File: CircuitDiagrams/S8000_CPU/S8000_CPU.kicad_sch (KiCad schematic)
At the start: 0 parts

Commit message: S8000 CPU schematics Page 3
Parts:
- added U27, U8: 7432, Package_DIP:DIP-14_W7.62mm, symbol 74xx:74LS32
- added U32: 7404, Package_DIP:DIP-14_W7.62mm, symbol 74xx:74LS04
- added U35: 7407, Package_DIP:DIP-14_W7.62mm, symbol 74xx:74LS07
- added U4: 7421, Package_DIP:DIP-14_W7.62mm, symbol 74xx:74LS21
- added U54: 7427, Package_DIP:DIP-14_W7.62mm, symbol 74xx:74LS27
- added U81: 7414, Package_DIP:DIP-14_W7.62mm, symbol 74xx:74LS14
- added U9: 7400, Package_DIP:DIP-14_W7.62mm, symbol 74xx:74LS00
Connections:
- net +5V: now also U27.14 (VCC), U32.14 (VCC), U35.14 (VCC), U4.14 (VCC), U54.14 (VCC), U8.14 (VCC), U81.14 (VCC), U9.14 (VCC)
- net GND: now also U27.7 (GND), U32.7 (GND), U35.7 (GND), U4.7 (GND), U54.7 (GND), U8.7 (GND), U81.7 (GND), U9.7 (GND)
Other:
- added sheet S8000 CPU 03 (S8000_CPU_03.kicad_sch)
- sheet S8000 CPU 02 ports: added none; removed ADIN[0..15], IAD[0..15], IST0, IST1, IST2, IST3, I~{DS}, SEGT

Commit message: Add Page 4
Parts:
- added U14: 74113, Package_DIP:DIP-14_W7.62mm, symbol 74xx:74LS113
- added U33: 7411, Package_DIP:DIP-14_W7.62mm, symbol 74xx:74LS11
- added U41, U42: 7432, Package_DIP:DIP-14_W7.62mm, symbol 74xx:74LS32
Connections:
- net +5V: now also U14.14 (VCC), U33.14 (VCC), U41.14 (VCC), U42.14 (VCC)
- net GND: now also U14.7 (GND), U33.7 (GND), U41.7 (GND), U42.7 (GND)
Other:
- added sheet S8000 CPU 04 (S8000_CPU_04.kicad_sch)
- sheet S8000 CPU 02 ports: added none; removed BUSACKH, BUS_B/~{W}, BUS_N/~{S}, BUS_R/~{W}, BUS_ST0, BUS_ST1, BUS_ST2, BUS_ST3, BUS_ST4, BUS_~{BUSACK}, BUS_~{NMI}, BUS_~{NVI}, BUS_~{REQ}, BUS_~{STOP}, BUS_~{VI}, BUS_~{WAIT}, B/~{W}, CLOCK, IAS, IB/~{W}, IDS, IN/~{S}, IR/~{W}, ISNAD[0..7], IW/~{B}, IW/~{R}, I~{AS}, LAD[0..15], R/~{W}, SN[0..6], ST0, ST1, ST2, ST3, ~{AS}, ~{BD DATAEN}, ~{BUSACK}, ~{DS}, ~{INT}, ~{IST3}, ~{MREQ}, ~{MRESET}, ~{RESET}, ~{SEGT}, ~{SEL_SN_VIOL_REG}, ~{WAIT}
- moved on the sheet: U27E, U32G, U35G

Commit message: Add Page 5 (SIO 0+1)
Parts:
- added U104, U127: 7404, symbol 74xx:74LS04
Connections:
- net +5V: now also U104.14 (VCC), U127.14 (VCC)
- net GND: now also U104.7 (GND), U127.7 (GND)
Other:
- added sheet S8000 CPU 05 (S8000_CPU_05.kicad_sch)
- moved on the sheet: U41E, U42E, U54D, U81G

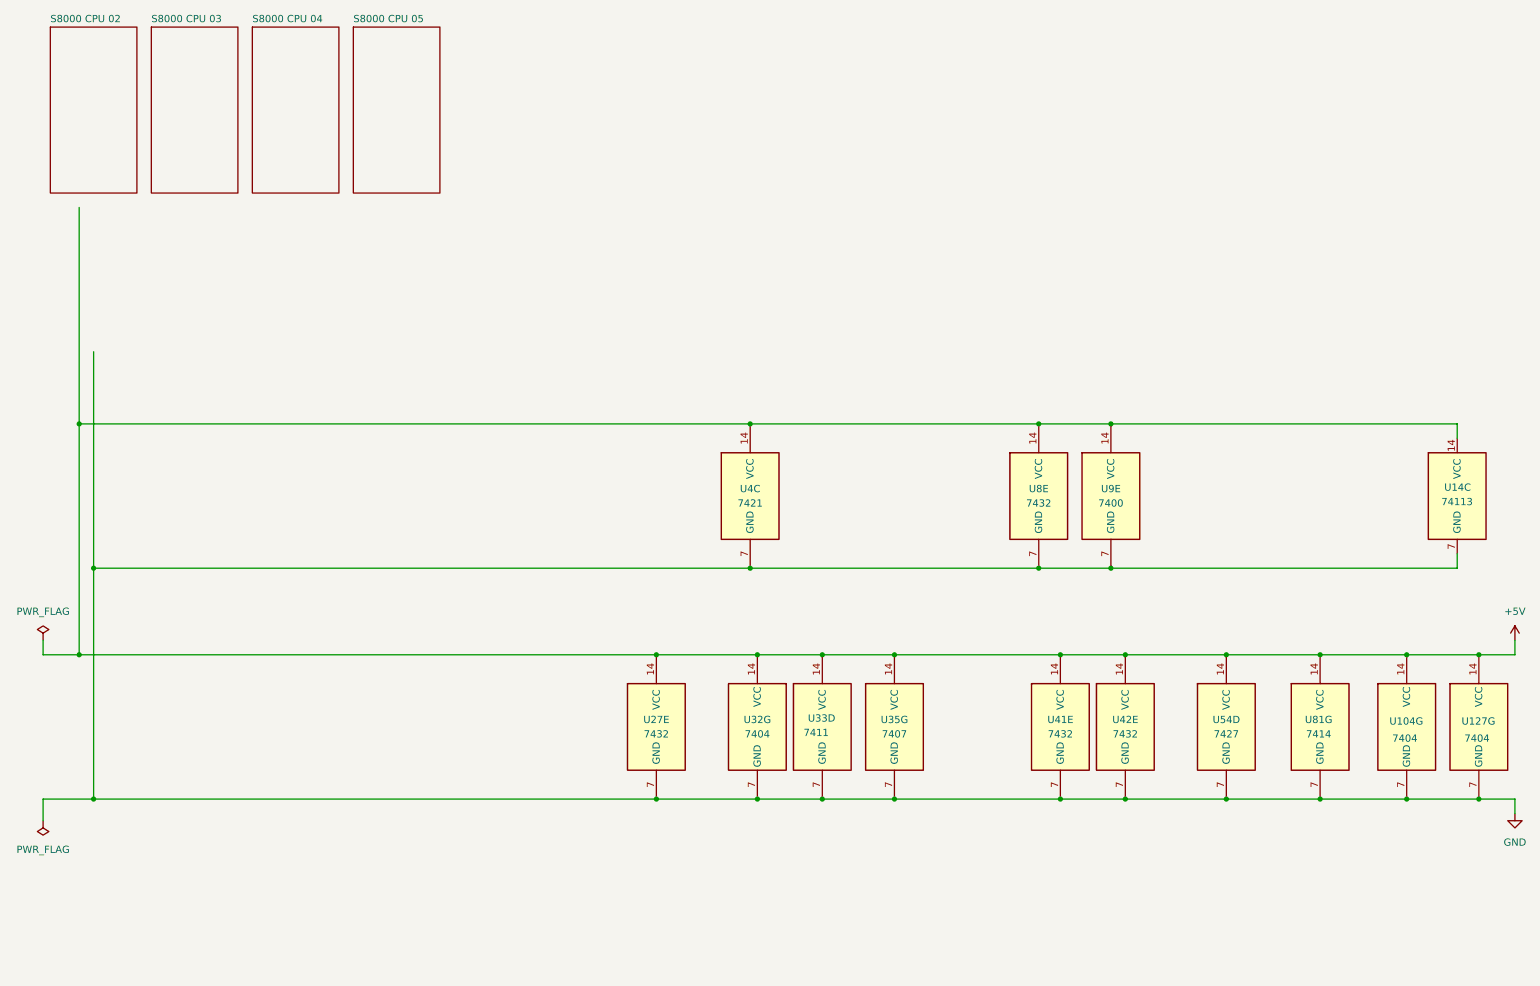
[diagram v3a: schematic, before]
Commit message: Add Page 6 (SIO 2+3)
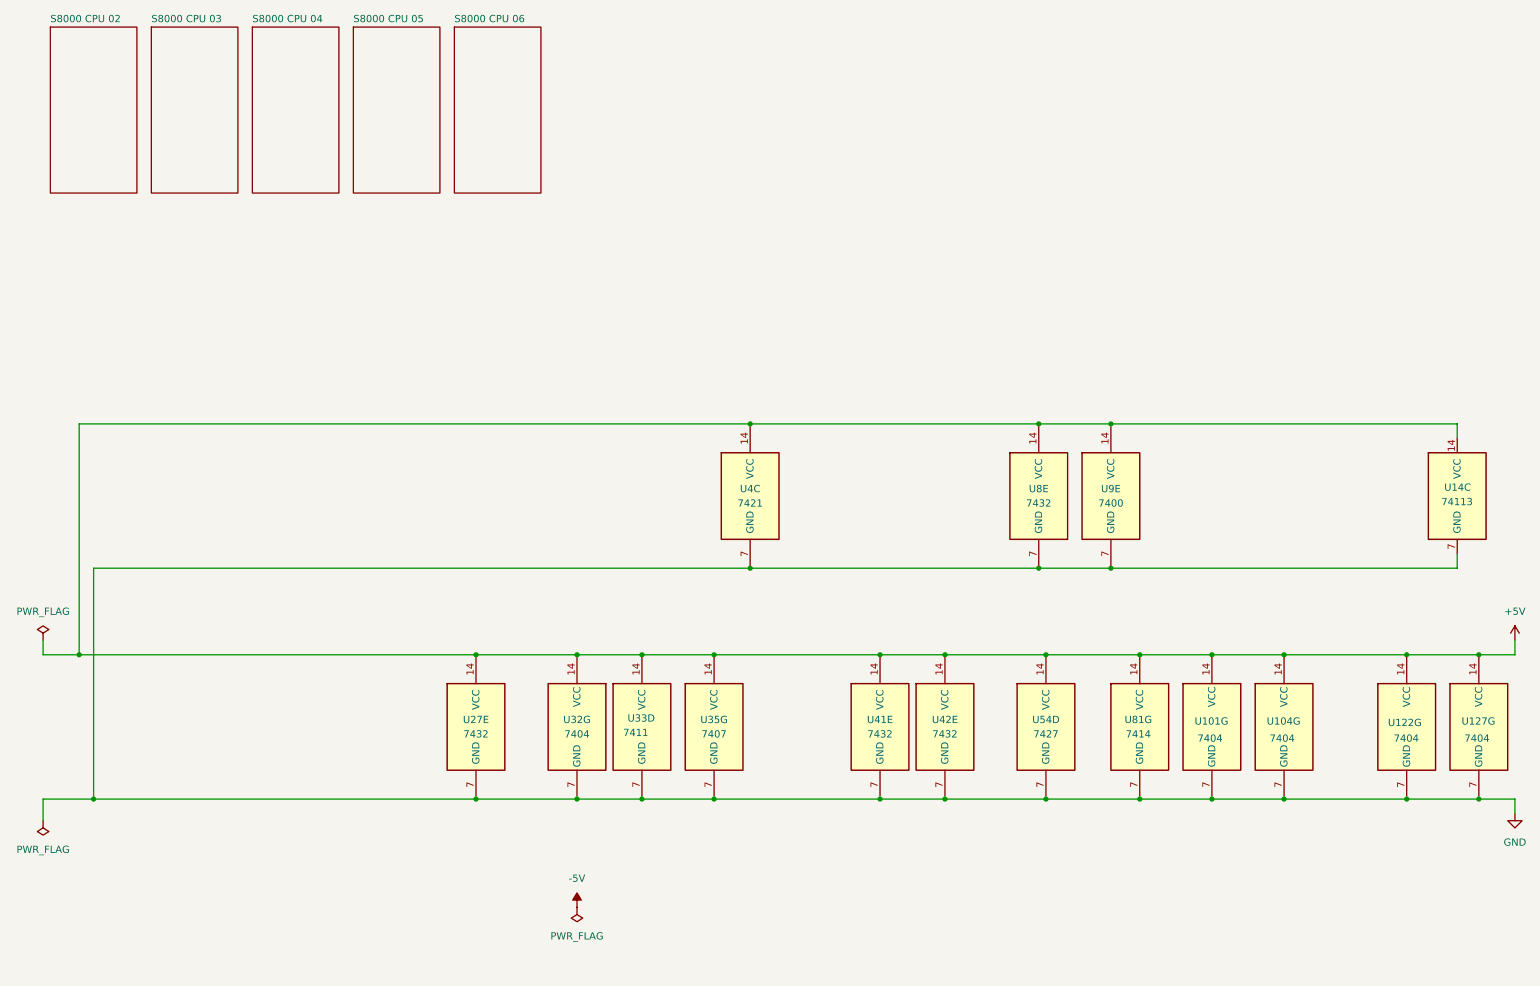
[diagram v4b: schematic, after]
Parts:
- added U101, U122: 7404, Package_DIP:DIP-14_W7.62mm, symbol 74xx:74LS04
- U104, U127: footprint (none) -> Package_DIP:DIP-14_W7.62mm
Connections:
- net +5V: now also U101.14 (VCC), U122.14 (VCC)
- net GND: now also U101.7 (GND), U122.7 (GND)
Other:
- added sheet S8000 CPU 06 (S8000_CPU_06.kicad_sch)
- moved on the sheet: U104G, U27E, U32G, U33D, U35G, U41E, U42E, U54D, U81G

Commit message: Add Page 6 (SIO 2+3), 7 (CTC 2 + PIO)
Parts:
- added U103: 74244, symbol S8000:74LS244
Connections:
- net +5V: now also U103.20 (VCC)
- net GND: now also U103.10 (GND)
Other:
- added sheet S8000 CPU 07 (S8000_CPU_07.kicad_sch)
- moved on the sheet: U101G, U41E, U42E, U54D, U81G

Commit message: Add Page 8 MMU (in progress)
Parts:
- added U11, U12: 74240, symbol 74xx:74LS240_Split
- added U13, U20: 74113, Package_DIP:DIP-14_W7.62mm, symbol 74xx:74LS113
- added U17: 7400, symbol 74xx:74LS00
- added U18: 7402, symbol 74xx:74LS02
- added U21: 7432, symbol 74xx:74LS32
- added U3: 7408, symbol 74xx:74LS08
- added U30: 7410, symbol 74xx:74LS10
- U42: value 7432 -> 7408
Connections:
- net +5V: now also U11.20 (VCC), U12.20 (VCC), U13.14 (VCC), U17.14 (VCC), U18.14 (VCC), U20.14 (VCC), U21.14 (VCC), U3.14 (VCC), U30.14 (VCC)
- net GND: now also U11.10 (GND), U12.10 (GND), U13.7 (GND), U17.7 (GND), U18.7 (GND), U20.7 (GND), U21.7 (GND), U3.7 (GND), U30.7 (GND)
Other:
- added sheet S8000 CPU 08 (S8000_CPU_08.kicad_sch)
- moved on the sheet: U14C, U27E, U8E, U9E

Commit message: finish Page 7 and 8
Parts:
- added U15: 74113, symbol 74xx:74LS113
- added U5: 7408, symbol 74xx:74LS08
- added U6: 7402, symbol 74xx:74LS02
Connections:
- net +5V: now also U15.14 (VCC), U5.14 (VCC), U6.14 (VCC)
- net GND: now also U15.7 (GND), U5.7 (GND), U6.7 (GND)
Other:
- moved on the sheet: U17E, U18E, U4C

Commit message: Footprints
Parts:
- U103, U11, U12: footprint (none) -> Package_DIP:DIP-20_W7.62mm
- U15, U17, U18, U21, U3, U30, U5, U6: footprint (none) -> Package_DIP:DIP-14_W7.62mm
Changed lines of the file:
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@@
 			)
 		)
-		(property "Footprint" ""
+		(property "Footprint" "Package_DIP:DIP-14_W7.62mm"
 			(at 156.21 99.06 0)
 			(hide yes)
@@
 			)
 		)
-		(property "Footprint" ""
+		(property "Footprint" "Package_DIP:DIP-14_W7.62mm"
 			(at 143.51 99.06 0)
 			(hide yes)
@@
 			)
 		)
-		(property "Footprint" ""
+		(property "Footprint" "Package_DIP:DIP-20_W7.62mm"
 			(at 207.01 99.06 0)
 			(hide yes)
@@
 			)
 		)
-		(property "Footprint" ""
+		(property "Footprint" "Package_DIP:DIP-20_W7.62mm"
 			(at 194.31 99.06 0)
 			(hide yes)
@@
 			)
 		)
-		(property "Footprint" ""
+		(property "Footprint" "Package_DIP:DIP-14_W7.62mm"
 			(at 72.39 139.7 0)
 			(hide yes)
@@
 			)
 		)
-		(property "Footprint" ""
+		(property "Footprint" "Package_DIP:DIP-14_W7.62mm"
 			(at 265.43 99.06 0)
 			(hide yes)
@@
 			)
 		)
-		(property "Footprint" ""
+		(property "Footprint" "Package_DIP:DIP-14_W7.62mm"
 			(at 118.11 99.06 0)
 			(hide yes)
@@
 			)
 		)
-		(property "Footprint" ""
+		(property "Footprint" "Package_DIP:DIP-14_W7.62mm"
 			(at 99.06 139.7 0)
 			(hide yes)
@@
 			)
 		)
-		(property "Footprint" ""
+		(property "Footprint" "Package_DIP:DIP-14_W7.62mm"
 			(at 252.73 99.06 0)
 			(hide yes)
@@
 			)
 		)
-		(property "Footprint" ""
+		(property "Footprint" "Package_DIP:DIP-14_W7.62mm"
 			(at 241.3 99.06 0)
 			(hide yes)
@@
 			)
 		)
-		(property "Footprint" ""
+		(property "Footprint" "Package_DIP:DIP-20_W7.62mm"
 			(at 223.52 139.7 0)
 			(hide yes)
